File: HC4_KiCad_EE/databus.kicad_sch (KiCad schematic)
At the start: 32 parts, among them IC5 74HC244, IC6 74HC377, IC7 4511, J2 Port_IN, J3 Port_A, SW1 SW_DIP_x04

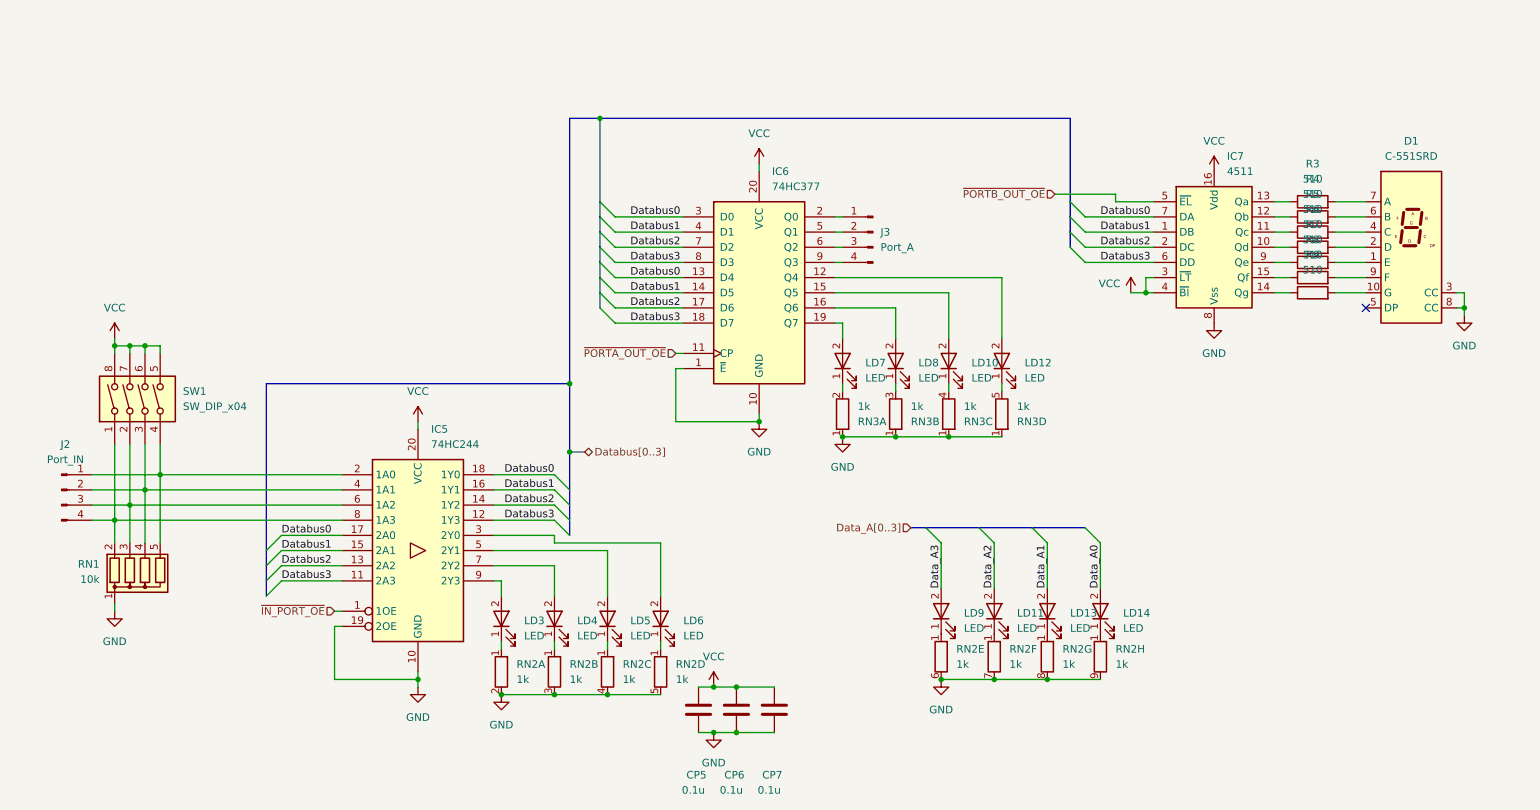
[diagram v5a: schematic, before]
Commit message: チップ集合抵抗に変更、基板作成開始
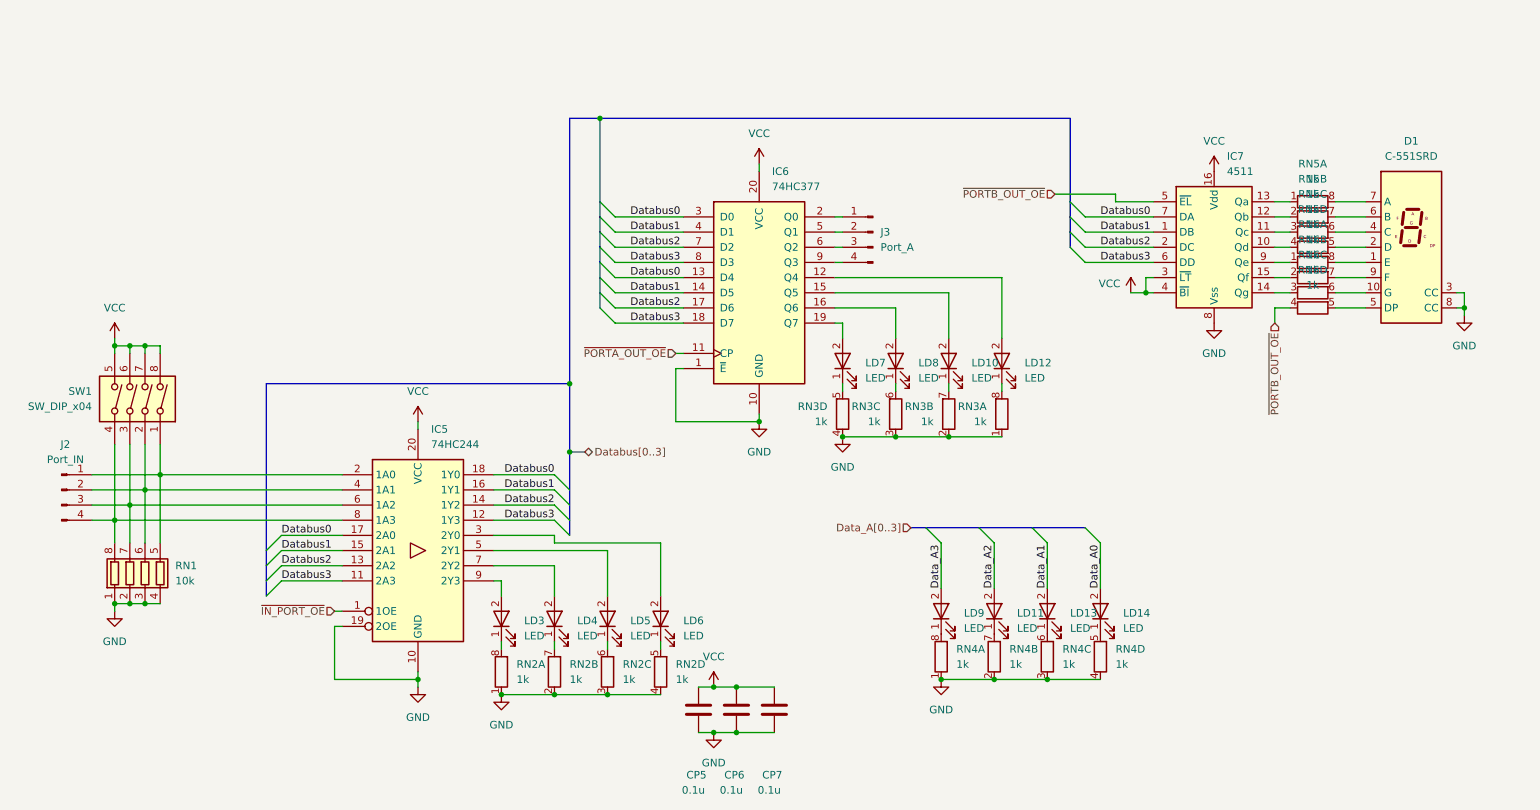
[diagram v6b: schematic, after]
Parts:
- removed R3, R4, R5, R6, R7, R8, R9: 510, symbol Device:R
- removed RN1: 10k, Resistor_THT:R_Array_SIP5, symbol Device:R_Network04
- removed RN2, RN3: 1k, Resistor_THT:R_Array_SIP9, symbol Device:R_Network08_Split
- added RN1: 10k, Resistor_SMD:R_Array_Convex_4x0603, symbol Device:R_Pack04
- added RN2, RN3, RN4, RN5, RN6: 1k, Resistor_SMD:R_Array_Convex_4x0603, symbol Device:R_Pack04_Split
- IC5, IC6: footprint Package_SO:SOP-20_7.5x12.8mm_P1.27mm -> Package_SO:TSSOP-20_4.4x6.5mm_P0.65mm
- IC7: footprint (none) -> Package_SO:SO-16_5.3x10.2mm_P1.27mm
- J2, J3: footprint (none) -> Connector_PinHeader_2.54mm:PinHeader_1x04_P2.54mm_Vertical
- SW1: footprint (none) -> Button_Switch_THT:SW_DIP_SPSTx04_Slide_9.78x12.34mm_W7.62mm_P2.54mm
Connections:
- net GND: now also RN1.1 (R1.1), RN1.2 (R2.1), RN1.3 (R3.1), RN1.4 (R4.1), RN2.1 (R1.1), RN2.2 (R2.1), RN2.3 (R3.1), RN2.4 (R4.1), RN3.1 (R1.1), RN3.2 (R2.1), RN3.3 (R3.1), RN3.4 (R4.1), RN4.1 (R1.1), RN4.2 (R2.1), RN4.3 (R3.1), RN4.4 (R4.1)
- net ~{PORTB_OUT_OE}: now also RN6.4 (R4.1)
- net at LD5.1 (K): now also RN2.6 (R3.2)
- net at LD11.1 (K): now also RN4.7 (R2.2)
- net at IC7.14 (Qg): now also RN6.3 (R3.1)
- net at D1.10 (G): now also RN6.6 (R3.2)
- net at LD13.1 (K): now also RN4.6 (R3.2)
- net at LD12.1 (K): now also RN3.8 (R1.2)
- net at IC5.8 (1A3), J2.4 (Pin_4): now also SW1.4, RN1.8 (R1.2); no longer SW1.1
- net at IC5.6 (1A2), J2.3 (Pin_3): now also SW1.3, RN1.7 (R2.2); no longer SW1.2
- net at IC5.4 (1A1), J2.2 (Pin_2): now also SW1.2, RN1.6 (R3.2); no longer SW1.3
- net at IC5.2 (1A0), J2.1 (Pin_1): now also SW1.1, RN1.5 (R4.2); no longer SW1.4
- net at LD6.1 (K): now also RN2.5 (R4.2)
- net at LD3.1 (K): now also RN2.8 (R1.2)
- net at D1.1 (E): now also RN6.8 (R1.2)
- net at D1.2 (D): now also RN5.5 (R4.2)
- net at D1.4 (C): now also RN5.6 (R3.2)
- net at D1.5 (DP): now also RN6.5 (R4.2)
- net at D1.6 (B): now also RN5.7 (R2.2)
- net at D1.7 (A): now also RN5.8 (R1.2)
- net at D1.9 (F): now also RN6.7 (R2.2)
- net at IC7.15 (Qf): now also RN6.2 (R2.1)
- net at LD8.1 (K): now also RN3.6 (R3.2)
- net at IC7.11 (Qc): now also RN5.3 (R3.1)
- net at LD10.1 (K): now also RN3.7 (R2.2)
- net at LD4.1 (K): now also RN2.7 (R2.2)
- net at LD14.1 (K): now also RN4.5 (R4.2)
- net at IC7.10 (Qd): now also RN5.4 (R4.1)
- net at IC7.12 (Qb): now also RN5.2 (R2.1)
- net at IC7.13 (Qa): now also RN5.1 (R1.1)
- net at IC7.9 (Qe): now also RN6.1 (R1.1)
- net at LD7.1 (K): now also RN3.5 (R4.2)
- net at LD9.1 (K): now also RN4.8 (R1.2)
- no-connect marks 1 -> 0
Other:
- moved on the sheet: SW1

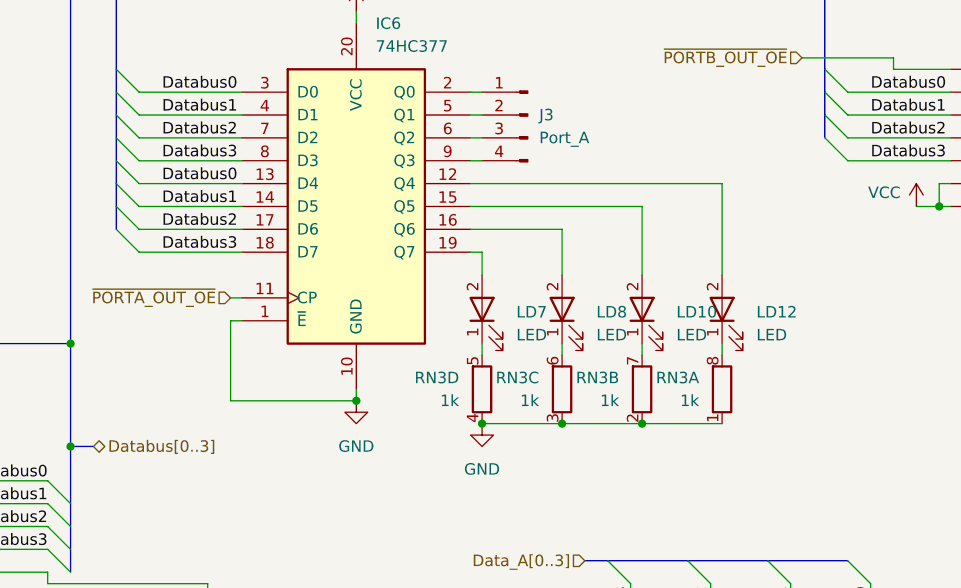
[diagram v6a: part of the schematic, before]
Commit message: 配線進捗、7474を使った変な回路
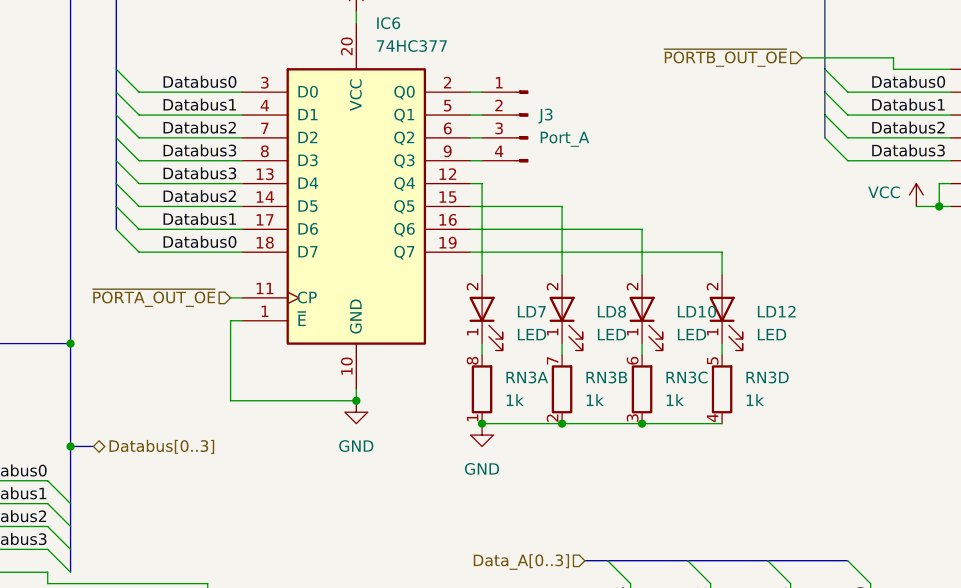
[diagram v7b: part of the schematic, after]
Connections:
- net Databus0: now also IC6.18 (D7); no longer IC6.13 (D4)
- net Databus1: now also IC6.17 (D6); no longer IC6.14 (D5)
- net Databus2: now also IC6.14 (D5); no longer IC6.17 (D6)
- net Databus3: now also IC6.13 (D4); no longer IC6.18 (D7)
- net at RN3.8 (R1.2): now also LD7.1 (K); no longer LD12.1 (K)
- net at RN3.6 (R3.2): now also LD10.1 (K); no longer LD8.1 (K)
- net at RN3.7 (R2.2): now also LD8.1 (K); no longer LD10.1 (K)
- net at LD12.2: now also IC6.19 (Q7); no longer IC6.12 (Q4)
- net at IC6.15 (Q5): now also LD8.2; no longer LD10.2
- net at IC6.16 (Q6): now also LD10.2; no longer LD8.2
- net at LD7.2: now also IC6.12 (Q4); no longer IC6.19 (Q7)
- net at RN3.5 (R4.2): now also LD12.1 (K); no longer LD7.1 (K)
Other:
- moved on the sheet: RN3A, RN3B, RN3C, RN3D

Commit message: 振出しに戻る
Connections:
- net Databus0: now also IC6.13 (D4), IC6.8 (D3); no longer IC6.18 (D7), IC6.3 (D0)
- net Databus1: now also IC6.14 (D5), IC6.7 (D2); no longer IC6.17 (D6), IC6.4 (D1)
- net Databus2: now also IC6.17 (D6), IC6.4 (D1); no longer IC6.14 (D5), IC6.7 (D2)
- net Databus3: now also IC6.18 (D7), IC6.3 (D0); no longer IC6.13 (D4), IC6.8 (D3)
- net at LD12.2: now also IC6.12 (Q4); no longer IC6.19 (Q7)
- net at LD7.2: now also IC6.19 (Q7); no longer IC6.12 (Q4)
- net at IC6.15 (Q5): now also LD10.2; no longer LD8.2
- net at IC6.16 (Q6): now also LD8.2; no longer LD10.2
- net at IC6.2 (Q0): now also J3.4 (Pin_4); no longer J3.1 (Pin_1)
- net at IC6.5 (Q1): now also J3.3 (Pin_3); no longer J3.2 (Pin_2)
- net at IC6.6 (Q2): now also J3.2 (Pin_2); no longer J3.3 (Pin_3)
- net at IC6.9 (Q3): now also J3.1 (Pin_1); no longer J3.4 (Pin_4)
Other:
- moved on the sheet: J3
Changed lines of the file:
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@@
 		)
 	)
-	(wire
-		(pts
-			(xy 179.07 90.17) (xy 179.07 97.79)
-		)
-		(stroke
-			(width 0)
-			(type default)
-		)
-	)
 	(bus
 		(pts
@@
 	(wire
 		(pts
+			(xy 168.91 95.25) (xy 170.18 95.25)
+		)
+		(stroke
+			(width 0)
+			(type default)
+		)
+	)
+	(wire
+		(pts
 			(xy 143.51 102.87) (xy 142.24 102.87)
 		)
@@
 	(wire
 		(pts
-			(xy 146.05 163.83) (xy 148.59 163.83)
+			(xy 196.85 87.63) (xy 196.85 97.79)
 		)
 		(stroke
@@
 	(wire
 		(pts
-			(xy 44.45 120.65) (xy 55.88 120.65)
+			(xy 146.05 163.83) (xy 148.59 163.83)
 		)
 		(stroke
@@
 	(wire
 		(pts
-			(xy 86.36 135.89) (xy 76.2 135.89)
+			(xy 44.45 120.65) (xy 55.88 120.65)
 		)
 		(stroke
@@
 	(wire
 		(pts
-			(xy 168.91 95.25) (xy 196.85 95.25)
+			(xy 86.36 135.89) (xy 76.2 135.89)
 		)
 		(stroke
@@
 	(wire
 		(pts
-			(xy 168.91 92.71) (xy 187.96 92.71)
-		)
-		(stroke
-			(width 0)
-			(type default)
-		)
-	)
-	(wire
-		(pts
 			(xy 85.09 154.94) (xy 99.06 154.94)
 		)
@@
 	(wire
 		(pts
+			(xy 168.91 90.17) (xy 187.96 90.17)
+		)
+		(stroke
+			(width 0)
+			(type default)
+		)
+	)
+	(wire
+		(pts
 			(xy 111.76 130.81) (xy 121.92 130.81)
 		)
@@
 	(wire
 		(pts
-			(xy 187.96 92.71) (xy 187.96 97.79)
+			(xy 187.96 90.17) (xy 187.96 97.79)
 		)
 		(stroke
@@
 	(wire
 		(pts
-			(xy 170.18 87.63) (xy 168.91 87.63)
+			(xy 168.91 87.63) (xy 196.85 87.63)
 		)
 		(stroke
@@
 	(wire
 		(pts
+			(xy 168.91 92.71) (xy 179.07 92.71)
+		)
+		(stroke
+			(width 0)
+			(type default)
+		)
+	)
+	(wire
+		(pts
 			(xy 156.21 111.76) (xy 156.21 110.49)
 		)
@@
 		)
 	)
+	(wire
+		(pts
+			(xy 179.07 92.71) (xy 179.07 97.79)
+		)
+		(stroke
+			(width 0)
+			(type default)
+		)
+	)
 	(bus
 		(pts
@@
 	(wire
 		(pts
-			(xy 53.34 100.33) (xy 53.34 99.06)
+			(xy 170.18 95.25) (xy 170.18 97.79)
 		)
 		(stroke
@@
 		)
 	)
-	(bus
+	(wire
 		(pts
-			(xy 124.46 128.27) (xy 124.46 130.81)
+			(xy 53.34 100.33) (xy 53.34 99.06)
 		)
 		(stroke
@@
 	(bus
 		(pts
-			(xy 73.66 105.41) (xy 124.46 105.41)
+			(xy 124.46 128.27) (xy 124.46 130.81)
 		)
 		(stroke
@@
 		)
 	)
-	(wire
+	(bus
 		(pts
-			(xy 170.18 87.63) (xy 170.18 97.79)
+			(xy 73.66 105.41) (xy 124.46 105.41)
 		)
 		(stroke
@@
 	(wire
 		(pts
-			(xy 196.85 95.25) (xy 196.85 97.79)
-		)
-		(stroke
-			(width 0)
-			(type default)
-		)
-	)
-	(wire
-		(pts
 			(xy 274.32 93.98) (xy 274.32 92.71)
 		)
@@
 	(wire
 		(pts
-			(xy 168.91 90.17) (xy 179.07 90.17)
-		)
-		(stroke
-			(width 0)
-			(type default)
-		)
-	)
-	(wire
-		(pts
 			(xy 148.59 163.83) (xy 152.4 163.83)
 		)
@@
 	)
 	(label "Databus2"
-		(at 134.62 90.17 0)
+		(at 134.62 80.01 0)
 		(effects
 			(font
@@
 	)
 	(label "Databus2"
-		(at 134.62 82.55 0)
+		(at 134.62 92.71 0)
 		(effects
 			(font
@@
 	)
 	(label "Databus3"
-		(at 134.62 87.63 0)
+		(at 134.62 77.47 0)
 		(effects
 			(font
@@
 	)
 	(label "Databus1"
-		(at 134.62 80.01 0)
+		(at 134.62 90.17 0)
 		(effects
 			(font
@@
 	)
 	(label "Databus3"
-		(at 134.62 85.09 0)
+		(at 134.62 95.25 0)
 		(effects
 			(font
@@
 	)
 	(label "Databus0"
-		(at 134.62 95.25 0)
+		(at 134.62 85.09 0)
 		(effects
 			(font
@@
 	)
 	(label "Databus1"
-		(at 134.62 92.71 0)
+		(at 134.62 82.55 0)
 		(effects
 			(font
@@
 	)
 	(label "Databus0"
-		(at 134.62 77.47 0)
+		(at 134.62 87.63 0)
 		(effects
 			(font
@@
 	(symbol
 		(lib_id "Connector:Conn_01x04_Pin")
-		(at 175.26 80.01 0)
-		(mirror y)
+		(at 175.26 82.55 180)
 		(unit 1)
 		(exclude_from_sim no)
@@
 		(on_board yes)
 		(dnp no)
-		(fields_autoplaced yes)
 		(property "Reference" "J3"
-			(at 176.53 80.0099 0)
+			(at 176.53 82.5501 0)
 			(effects
 				(font
@@
 		)
 		(property "Value" "Port_A"
-			(at 176.53 82.5499 0)
+			(at 176.53 80.0101 0)
 			(effects
 				(font
@@
 		)
 		(property "Footprint" "Connector_PinHeader_2.54mm:PinHeader_1x04_P2.54mm_Vertical"
-			(at 175.26 80.01 0)
+			(at 175.26 82.55 0)
 			(effects
 				(font
@@
 		)
 		(property "Datasheet" "~"
-			(at 175.26 80.01 0)
+			(at 175.26 82.55 0)
 			(effects
 				(font
@@
 		)
 		(property "Description" "Generic connector, single row, 01x04, script generated"
-			(at 175.26 80.01 0)
+			(at 175.26 82.55 0)
 			(effects
 				(font
